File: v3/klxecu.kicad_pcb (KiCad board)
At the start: 4 copper layers, 80.3 x 86.4 mm, 131 parts, among them IC1 SP721, J1 cam_sensor, J2 Conn_01x06, J3 DIP8, J4 Conn_02x04_Counter_Clockwise, J5 TACH_OUT, J6 IGN_ARD_OUT, J7 IGN_DRV_OUT, J8 IGN_CONN, Q1 SSM3K357R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

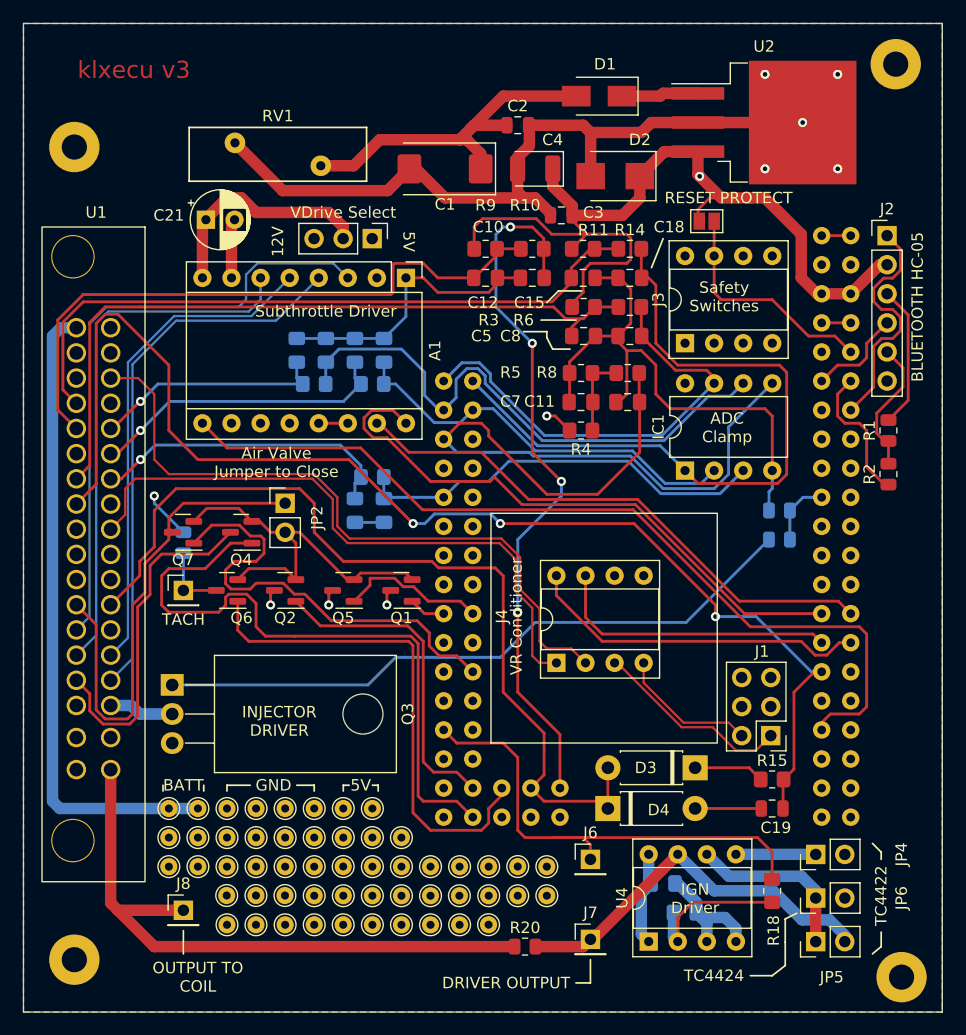
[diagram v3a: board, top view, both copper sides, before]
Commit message: change kill switch circuitry
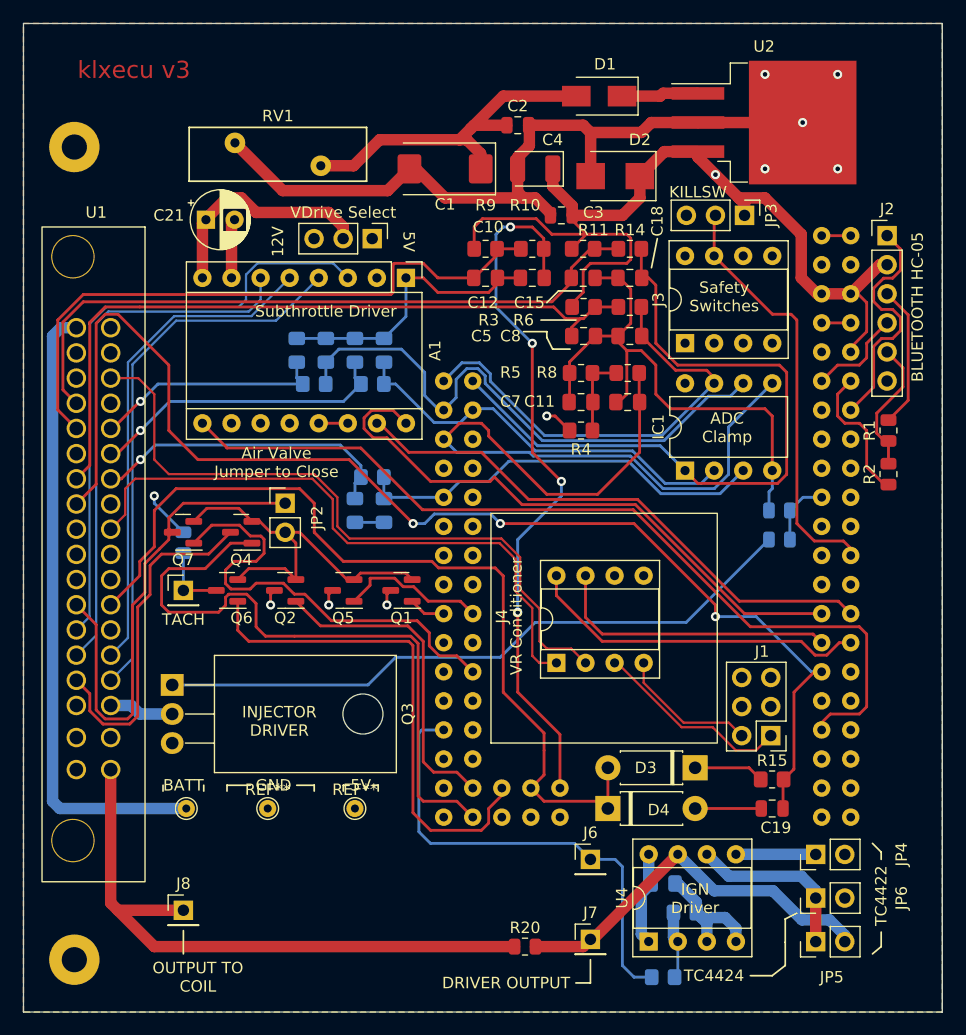
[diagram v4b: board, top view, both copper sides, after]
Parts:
- removed the REF** at (45.7, 101.6)
- removed the REF** at (71.1, 109.2)
- removed the REF** at (66.0, 106.7)
- removed the REF** at (55.9, 109.2)
- removed the REF** at (48.3, 104.1)
- removed the REF** at (48.3, 101.6)
- removed the REF** at (58.4, 106.7)
- removed the REF** at (38.1, 106.7)
- removed the REF** at (102.1, 116.3)
- removed the REF** at (53.3, 111.8)
- removed the REF** at (45.7, 109.2)
- removed the REF** at (55.9, 104.1)
- removed the REF** at (61.0, 111.8)
- removed the REF** at (48.3, 111.8)
- removed the REF** at (68.6, 106.7)
- removed the REF** at (40.6, 104.1)
- removed the REF** at (58.4, 104.1)
- removed the REF** at (45.7, 106.7)
- removed the REF** at (53.3, 104.1)
- removed the REF** at (50.8, 106.7)
- removed the REF** at (43.2, 106.7)
- removed the REF** at (38.1, 101.6)
- removed the REF** at (61.0, 109.2)
- removed the REF** at (50.8, 111.8)
- removed the REF** at (55.9, 101.6)
- removed the REF** at (48.2, 109.2)
- removed the REF** at (55.9, 111.8)
- removed the REF** at (55.9, 106.7)
- removed the REF** at (43.2, 101.6)
- removed the REF** at (68.6, 109.2)
- removed the REF** at (63.5, 109.2)
- removed the REF** at (58.4, 109.2)
- removed the REF** at (61.0, 106.7)
- removed the REF** at (50.8, 104.1)
- removed the REF** at (38.1, 104.1)
- removed the REF** at (43.2, 104.1)
- removed the REF** at (101.6, 36.6)
- removed the REF** at (53.3, 109.2)
- removed the REF** at (53.3, 106.7)
- removed the REF** at (58.4, 111.8)
- removed the REF** at (63.5, 106.7)
- removed the REF** at (45.7, 111.8)
- removed the REF** at (53.3, 101.6)
- removed the REF** at (45.7, 104.1)
- removed the REF** at (66.0, 111.8)
- removed the REF** at (50.8, 101.6)
- removed the REF** at (40.6, 101.6)
- removed the REF** at (63.5, 111.8)
- removed the REF** at (43.2, 111.8)
- removed the REF** at (43.2, 109.2)
- removed the REF** at (71.1, 106.7)
- removed the REF** at (66.0, 109.2)
- removed the REF** at (48.3, 106.7)
- removed the REF** at (50.8, 109.2)
- removed the REF** at (40.6, 106.7)
- added REF**: TestPoint_THTPad_D1.5mm_Drill0.7mm, TestPoint:TestPoint_THTPad_D1.5mm_Drill0.7mm, F.Cu at (39.6, 101.6)
- added REF**: TestPoint_THTPad_D1.5mm_Drill0.7mm, TestPoint:TestPoint_THTPad_D1.5mm_Drill0.7mm, F.Cu at (46.7, 101.6)
- added REF**: TestPoint_THTPad_D1.5mm_Drill0.7mm, TestPoint:TestPoint_THTPad_D1.5mm_Drill0.7mm, F.Cu at (54.4, 101.6)
- JP3: value Jumper_2_Open -> Jumper_3_Open; footprint Jumper:SolderJumper-2_P1.3mm_Open_Pad1.0x1.5mm -> Connector_PinHeader_2.54mm:PinHeader_1x03_P2.54mm_Vertical
- R18: moved to B.Cu
- moved R18 12.2 mm to (81.3, 116.3), turned to 0 degrees
- moved JP3 3.34 mm to (88.4, 49.8), turned to -90 degrees
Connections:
- net ARD-D3 renamed EN-ARD-D3
- J3 pad 4: VDOWN -> GND
- J3 pad 6: unconnected-(J3-Pad6) -> VDOWN
- J3 pad 7: ARDUINO-RST -> KILLSW-ARD-D13
- J3 pad 8: GND -> +5V
- JP3 pad 2: ARDUINO-RST -> KILLSW-ARD-D13
- U3 pad D13: unconnected-(U3-PadD13) -> KILLSW-ARD-D13
- U3 pad RST: ARDUINO-RST -> +5V
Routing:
- net KILLSW-ARD-D13: track 0.00 -> 36.6 mm
- net ARDUINO-RST: track 20.3 -> 0.00 mm
- net VDOWN: track 61.2 -> 77.8 mm
- net Net-(R18-Pad2): track 13.6 -> 5.91 mm
- net +5V: track 95.5 -> 99.5 mm
- net IGN-ARD-D40: track 43.9 -> 41.6 mm
- net +BATT: track 56.0 -> 55.0 mm
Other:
- board text added: "KILLSW"
- board text removed: "RESET PROTECT"
